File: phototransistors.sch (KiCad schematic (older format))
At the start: 15 parts

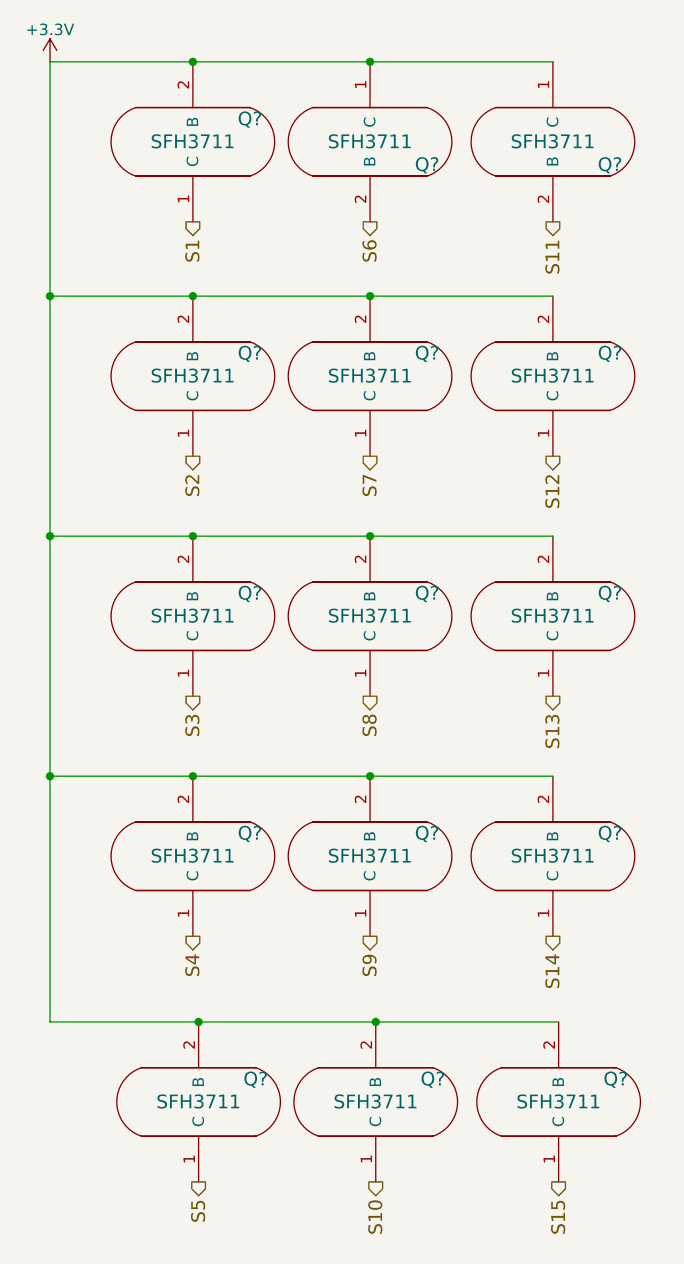
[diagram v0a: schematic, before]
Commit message: Progress on schematic, phototransistor array + analog frontend complete
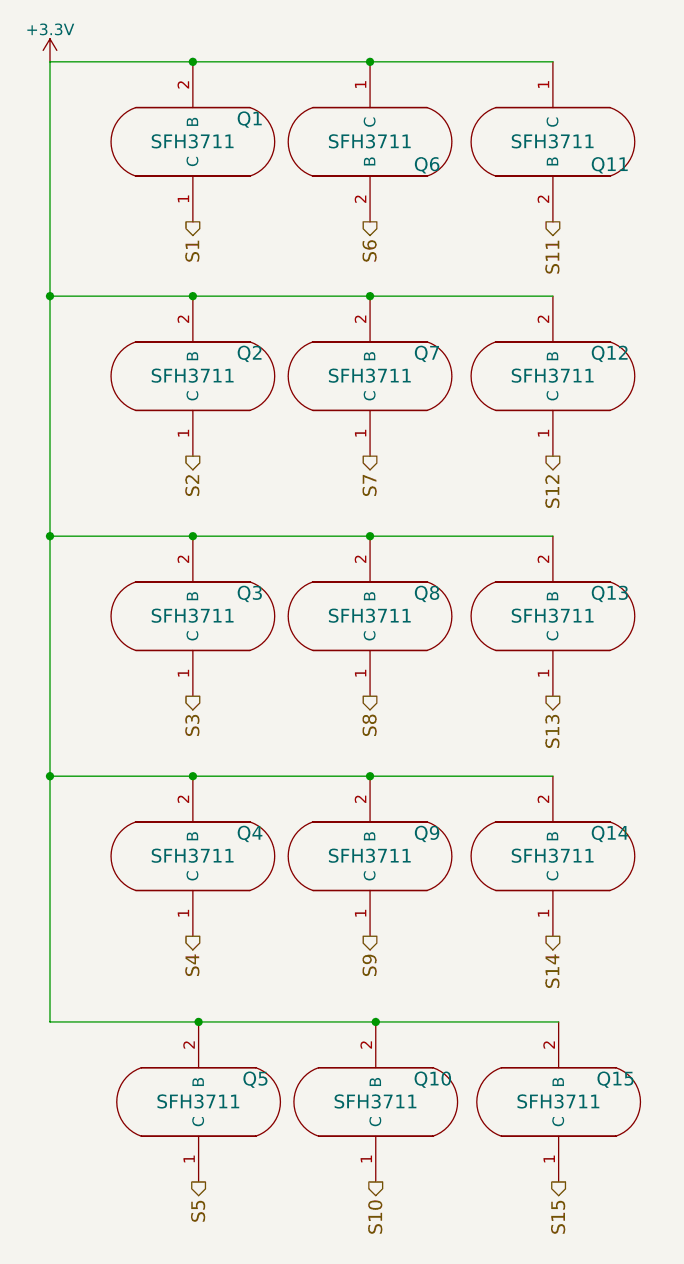
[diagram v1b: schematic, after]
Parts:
- Q1, Q10, Q11, Q12, Q13, Q14, Q15, Q2, Q3, Q4, Q5, Q6, Q7, Q8, Q9: renamed from Q?; footprint (none) -> Resistors_SMD:R_0805_HandSoldering
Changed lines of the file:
@@
 $EndDescr
 $Comp
-L SFH3711 Q?
+L SFH3711 Q1
 U 1 1 56B94958
 P 2825 1950
-F 0 "Q?" H 3075 2100 60  0000 C CNN
+F 0 "Q1" H 3075 2100 60  0000 C CNN
 F 1 "SFH3711" H 2825 2200 60  0000 C CNN
-F 2 "" H 2825 2250 60  0000 C CNN
+F 2 "Resistors_SMD:R_0805_HandSoldering" H 2825 2250 60  0001 C CNN
 F 3 "" H 2825 2250 60  0000 C CNN
 	1    2825 1950
@@
 $EndComp
 $Comp
-L +3.3V #PWR?
+L +3.3V #PWR1
 U 1 1 56B94A02
 P 2200 1850
-F 0 "#PWR?" H 2200 1700 50  0001 C CNN
+F 0 "#PWR1" H 2200 1700 50  0001 C CNN
 F 1 "+3.3V" H 2200 1990 50  0000 C CNN
 F 2 "" H 2200 1850 50  0000 C CNN
@@
 $EndComp
 $Comp
-L SFH3711 Q?
+L SFH3711 Q6
 U 1 1 56B94A26
 P 3600 2450
-F 0 "Q?" H 3850 2600 60  0000 C CNN
+F 0 "Q6" H 3850 2600 60  0000 C CNN
 F 1 "SFH3711" H 3600 2700 60  0000 C CNN
-F 2 "" H 3600 2750 60  0000 C CNN
+F 2 "Resistors_SMD:R_0805_HandSoldering" H 3600 2750 60  0001 C CNN
 F 3 "" H 3600 2750 60  0000 C CNN
 	1    3600 2450
@@
 $EndComp
 $Comp
-L SFH3711 Q?
+L SFH3711 Q11
 U 1 1 56B94A86
 P 4400 2450
-F 0 "Q?" H 4650 2600 60  0000 C CNN
+F 0 "Q11" H 4650 2600 60  0000 C CNN
 F 1 "SFH3711" H 4400 2700 60  0000 C CNN
-F 2 "" H 4400 2750 60  0000 C CNN
+F 2 "Resistors_SMD:R_0805_HandSoldering" H 4400 2750 60  0001 C CNN
 F 3 "" H 4400 2750 60  0000 C CNN
 	1    4400 2450
@@
 $EndComp
 $Comp
-L SFH3711 Q?
+L SFH3711 Q2
 U 1 1 56B94C7F
 P 2825 2975
-F 0 "Q?" H 3075 3125 60  0000 C CNN
+F 0 "Q2" H 3075 3125 60  0000 C CNN
 F 1 "SFH3711" H 2825 3225 60  0000 C CNN
-F 2 "" H 2825 3275 60  0000 C CNN
+F 2 "Resistors_SMD:R_0805_HandSoldering" H 2825 3275 60  0001 C CNN
 F 3 "" H 2825 3275 60  0000 C CNN
 	1    2825 2975
@@
 $EndComp
 $Comp
-L SFH3711 Q?
+L SFH3711 Q7
 U 1 1 56B94CFB
 P 3600 2975
-F 0 "Q?" H 3850 3125 60  0000 C CNN
+F 0 "Q7" H 3850 3125 60  0000 C CNN
 F 1 "SFH3711" H 3600 3225 60  0000 C CNN
-F 2 "" H 3600 3275 60  0000 C CNN
+F 2 "Resistors_SMD:R_0805_HandSoldering" H 3600 3275 60  0001 C CNN
 F 3 "" H 3600 3275 60  0000 C CNN
 	1    3600 2975
@@
 $EndComp
 $Comp
-L SFH3711 Q?
+L SFH3711 Q12
 U 1 1 56B94D59
 P 4400 2975
-F 0 "Q?" H 4650 3125 60  0000 C CNN
+F 0 "Q12" H 4650 3125 60  0000 C CNN
 F 1 "SFH3711" H 4400 3225 60  0000 C CNN
-F 2 "" H 4400 3275 60  0000 C CNN
+F 2 "Resistors_SMD:R_0805_HandSoldering" H 4400 3275 60  0001 C CNN
 F 3 "" H 4400 3275 60  0000 C CNN
 	1    4400 2975
@@
 $EndComp
 $Comp
-L SFH3711 Q?
+L SFH3711 Q3
 U 1 1 56B94FE9
 P 2825 4025
-F 0 "Q?" H 3075 4175 60  0000 C CNN
+F 0 "Q3" H 3075 4175 60  0000 C CNN
 F 1 "SFH3711" H 2825 4275 60  0000 C CNN
-F 2 "" H 2825 4325 60  0000 C CNN
+F 2 "Resistors_SMD:R_0805_HandSoldering" H 2825 4325 60  0001 C CNN
 F 3 "" H 2825 4325 60  0000 C CNN
 	1    2825 4025
@@
 $EndComp
 $Comp
-L SFH3711 Q?
+L SFH3711 Q8
 U 1 1 56B94FEF
 P 3600 4025
-F 0 "Q?" H 3850 4175 60  0000 C CNN
+F 0 "Q8" H 3850 4175 60  0000 C CNN
 F 1 "SFH3711" H 3600 4275 60  0000 C CNN
-F 2 "" H 3600 4325 60  0000 C CNN
+F 2 "Resistors_SMD:R_0805_HandSoldering" H 3600 4325 60  0001 C CNN
 F 3 "" H 3600 4325 60  0000 C CNN
 	1    3600 4025
@@
 $EndComp
 $Comp
-L SFH3711 Q?
+L SFH3711 Q13
 U 1 1 56B94FF5
 P 4400 4025
-F 0 "Q?" H 4650 4175 60  0000 C CNN
+F 0 "Q13" H 4650 4175 60  0000 C CNN
 F 1 "SFH3711" H 4400 4275 60  0000 C CNN
-F 2 "" H 4400 4325 60  0000 C CNN
+F 2 "Resistors_SMD:R_0805_HandSoldering" H 4400 4325 60  0001 C CNN
 F 3 "" H 4400 4325 60  0000 C CNN
 	1    4400 4025
@@
 $EndComp
 $Comp
-L SFH3711 Q?
+L SFH3711 Q4
 U 1 1 56B950F7
 P 2825 5075
-F 0 "Q?" H 3075 5225 60  0000 C CNN
+F 0 "Q4" H 3075 5225 60  0000 C CNN
 F 1 "SFH3711" H 2825 5325 60  0000 C CNN
-F 2 "" H 2825 5375 60  0000 C CNN
+F 2 "Resistors_SMD:R_0805_HandSoldering" H 2825 5375 60  0001 C CNN
 F 3 "" H 2825 5375 60  0000 C CNN
 	1    2825 5075
@@
 $EndComp
 $Comp
-L SFH3711 Q?
+L SFH3711 Q9
 U 1 1 56B950FD
 P 3600 5075
-F 0 "Q?" H 3850 5225 60  0000 C CNN
+F 0 "Q9" H 3850 5225 60  0000 C CNN
 F 1 "SFH3711" H 3600 5325 60  0000 C CNN
-F 2 "" H 3600 5375 60  0000 C CNN
+F 2 "Resistors_SMD:R_0805_HandSoldering" H 3600 5375 60  0001 C CNN
 F 3 "" H 3600 5375 60  0000 C CNN
 	1    3600 5075
@@
 $EndComp
 $Comp
-L SFH3711 Q?
+L SFH3711 Q14
 U 1 1 56B95103
 P 4400 5075
-F 0 "Q?" H 4650 5225 60  0000 C CNN
+F 0 "Q14" H 4650 5225 60  0000 C CNN
 F 1 "SFH3711" H 4400 5325 60  0000 C CNN
-F 2 "" H 4400 5375 60  0000 C CNN
+F 2 "Resistors_SMD:R_0805_HandSoldering" H 4400 5375 60  0001 C CNN
 F 3 "" H 4400 5375 60  0000 C CNN
 	1    4400 5075
@@
 $EndComp
 $Comp
-L SFH3711 Q?
+L SFH3711 Q5
 U 1 1 56B951F6
 P 2850 6150
-F 0 "Q?" H 3100 6300 60  0000 C CNN
+F 0 "Q5" H 3100 6300 60  0000 C CNN
 F 1 "SFH3711" H 2850 6400 60  0000 C CNN
-F 2 "" H 2850 6450 60  0000 C CNN
+F 2 "Resistors_SMD:R_0805_HandSoldering" H 2850 6450 60  0001 C CNN
 F 3 "" H 2850 6450 60  0000 C CNN
 	1    2850 6150
@@
 $EndComp
 $Comp
-L SFH3711 Q?
+L SFH3711 Q10
 U 1 1 56B951FC
 P 3625 6150
-F 0 "Q?" H 3875 6300 60  0000 C CNN
+F 0 "Q10" H 3875 6300 60  0000 C CNN
 F 1 "SFH3711" H 3625 6400 60  0000 C CNN
-F 2 "" H 3625 6450 60  0000 C CNN
+F 2 "Resistors_SMD:R_0805_HandSoldering" H 3625 6450 60  0001 C CNN
 F 3 "" H 3625 6450 60  0000 C CNN
 	1    3625 6150
@@
 $EndComp
 $Comp
-L SFH3711 Q?
+L SFH3711 Q15
 U 1 1 56B95202
 P 4425 6150
-F 0 "Q?" H 4675 6300 60  0000 C CNN
+F 0 "Q15" H 4675 6300 60  0000 C CNN
 F 1 "SFH3711" H 4425 6400 60  0000 C CNN
-F 2 "" H 4425 6450 60  0000 C CNN
+F 2 "Resistors_SMD:R_0805_HandSoldering" H 4425 6450 60  0001 C CNN
 F 3 "" H 4425 6450 60  0000 C CNN
 	1    4425 6150

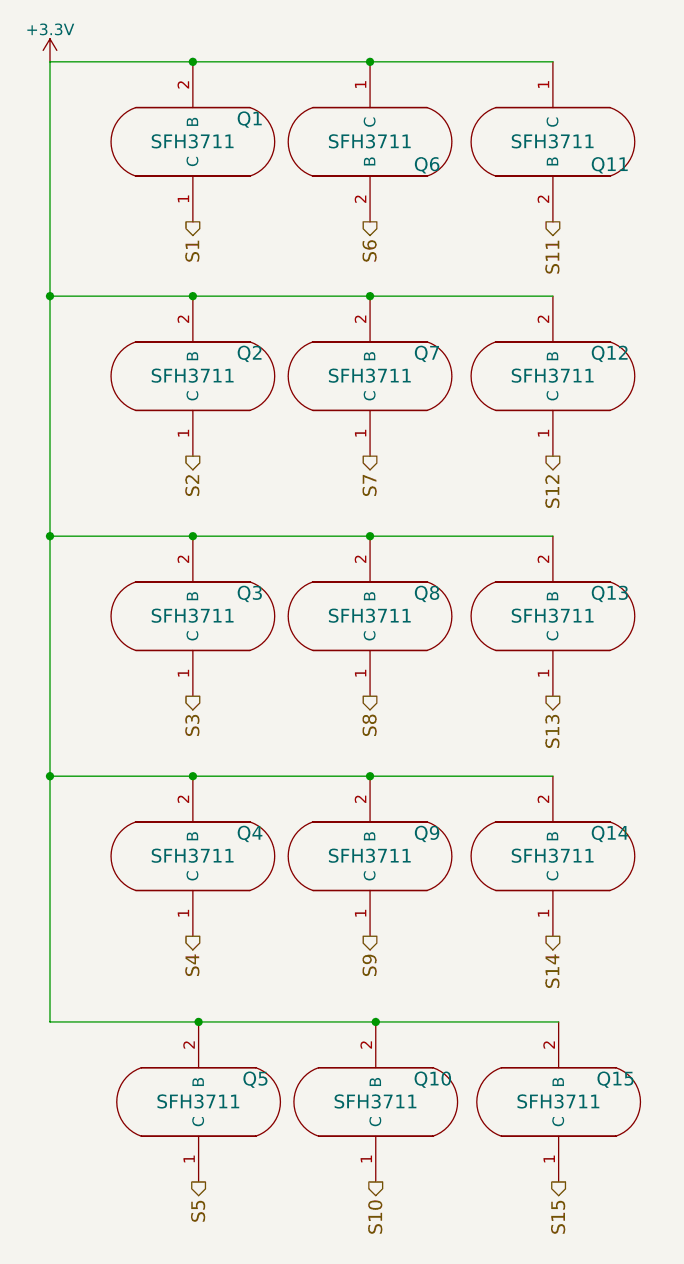
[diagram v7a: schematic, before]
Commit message: Changed schematic of SFH3710
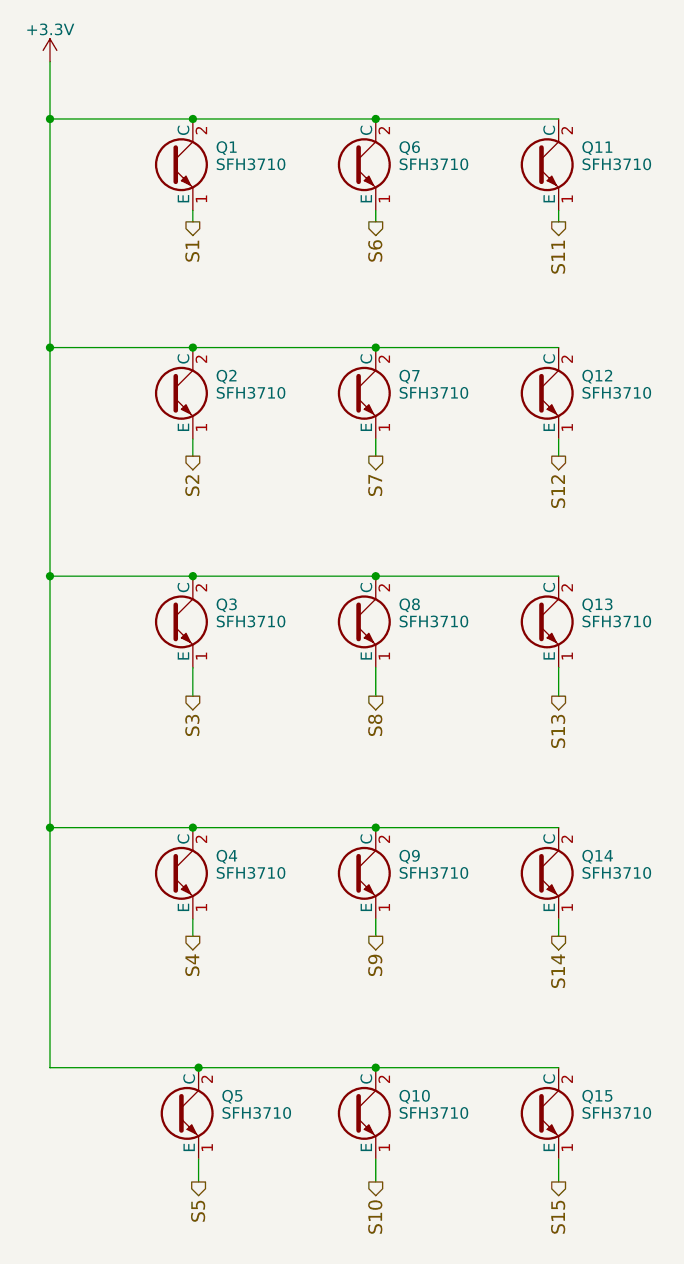
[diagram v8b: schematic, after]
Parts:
- removed Q1, Q10, Q11, Q12, Q13, Q14, Q15, Q2, Q3, Q4, Q5, Q6, Q7, Q8, Q9: SFH3711, Resistors_SMD:R_0805_HandSoldering, symbol SFH3711
- added Q1, Q10, Q11, Q12, Q13, Q14, Q15, Q2, Q3, Q4, Q5, Q6, Q7, Q8, Q9: SFH3710, Resistors_SMD:R_0805_HandSoldering, symbol SFH3710
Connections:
- net +3V3: now also Q1.2 (C), Q10.2 (C), Q11.2 (C), Q12.2 (C), Q13.2 (C), Q14.2 (C), Q15.2 (C), Q2.2 (C), Q3.2 (C), Q4.2 (C), Q5.2 (C), Q6.2 (C), Q7.2 (C), Q8.2 (C), Q9.2 (C)
- net S1: now also Q1.1 (E)
- net S10: now also Q10.1 (E)
- net S11: now also Q11.1 (E)
- net S12: now also Q12.1 (E)
- net S13: now also Q13.1 (E)
- net S14: now also Q14.1 (E)
- net S15: now also Q15.1 (E)
- net S2: now also Q2.1 (E)
- net S3: now also Q3.1 (E)
- net S4: now also Q4.1 (E)
- net S5: now also Q5.1 (E)
- net S6: now also Q6.1 (E)
- net S7: now also Q7.1 (E)
- net S8: now also Q8.1 (E)
- net S9: now also Q9.1 (E)
